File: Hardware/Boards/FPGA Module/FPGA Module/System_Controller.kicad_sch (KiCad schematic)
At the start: 32 parts, among them SW1 RST, U16 L78L33_SOT89, U5 W25Q16JVUXIQ TR, U6 RP2040, Y1 12Mhz

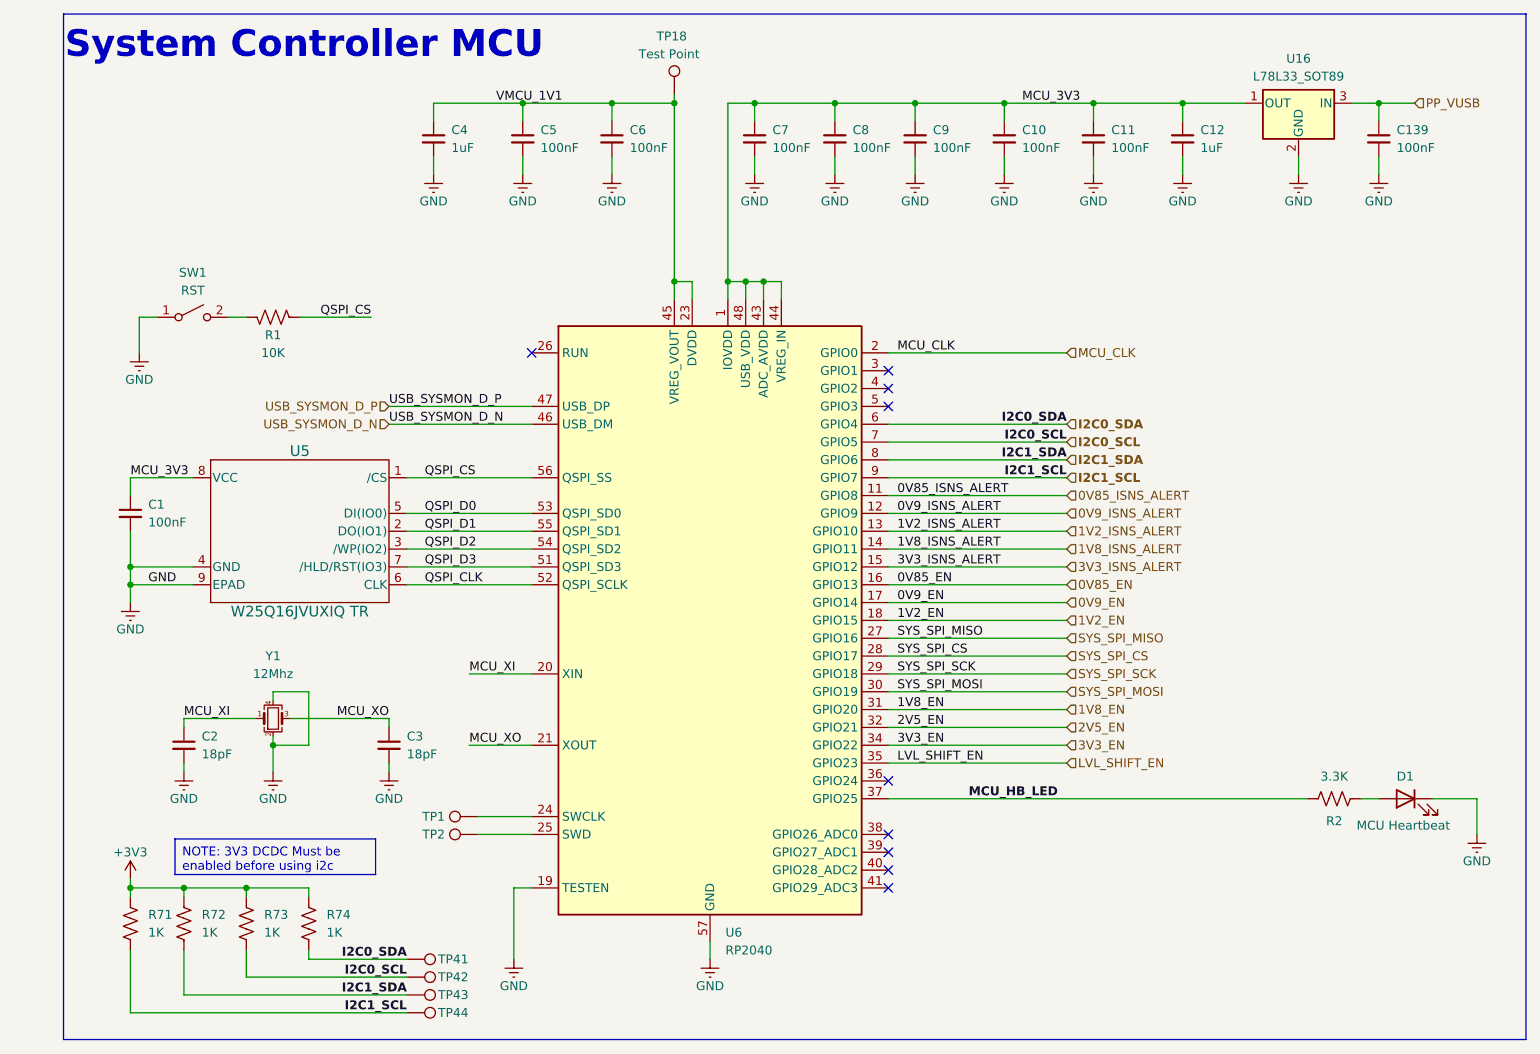
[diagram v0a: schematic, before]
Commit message: Completed FPGA module PCB layout
Started PCB routing
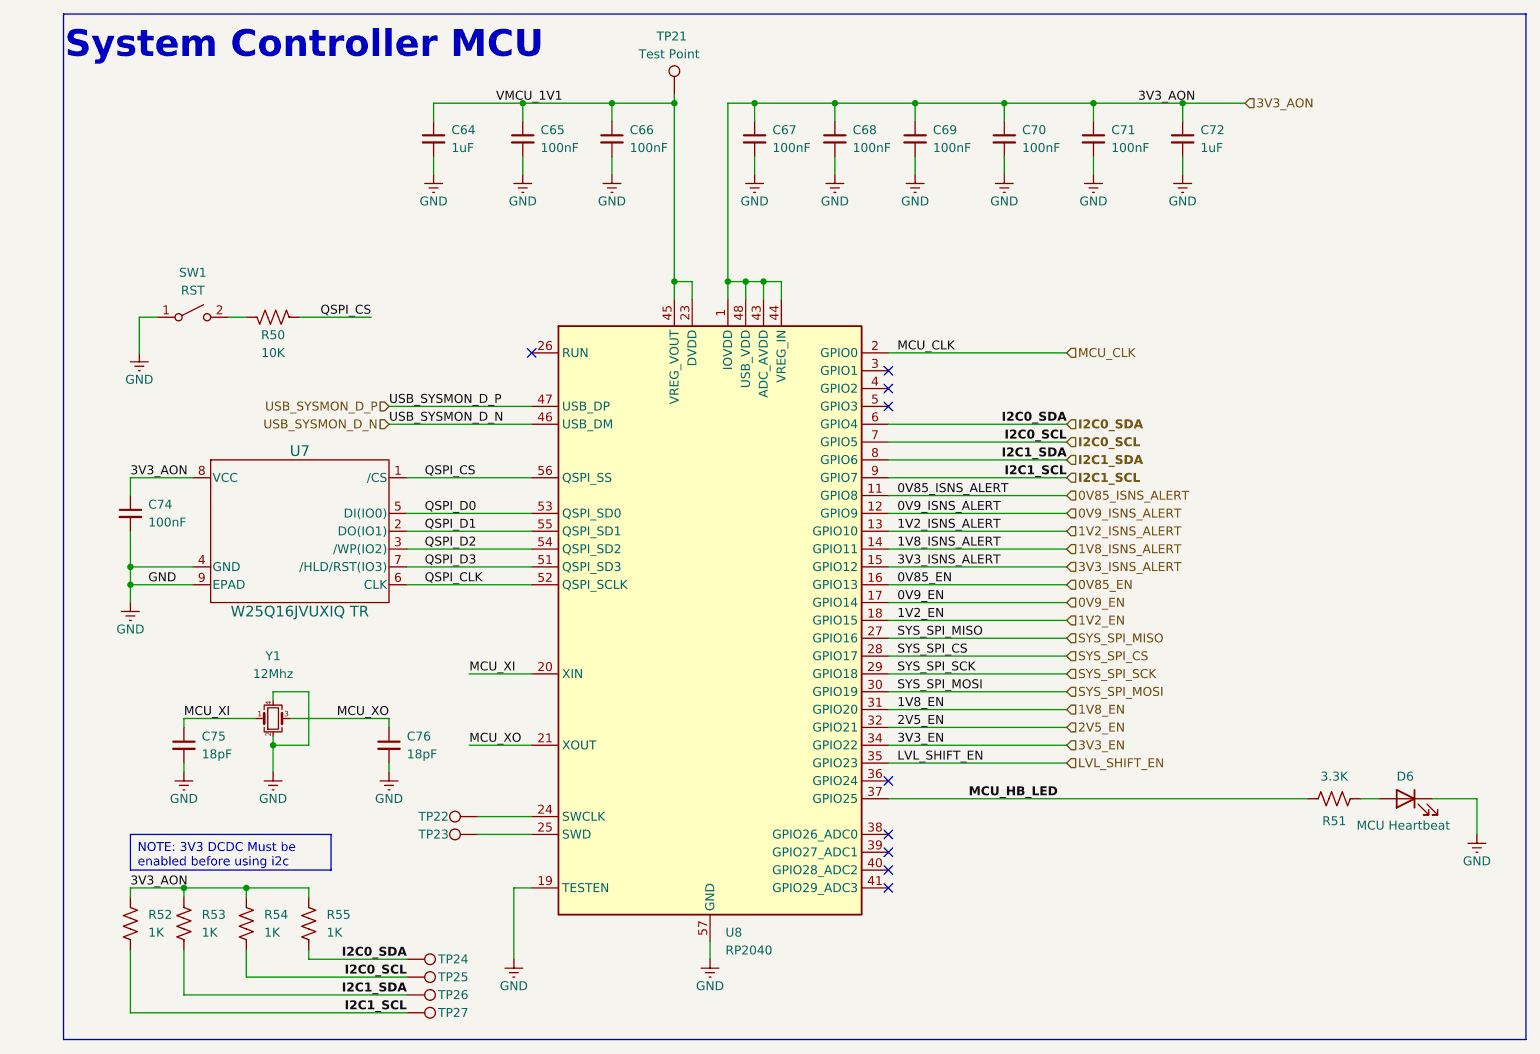
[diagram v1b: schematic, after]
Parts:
- removed C139: 100nF, Capacitor_SMD:C_0201_0603Metric, symbol Device:C_Small
- removed U16: L78L33_SOT89, Package_TO_SOT_SMD:SOT-89-3, symbol Regulator_Linear:L78L33_SOT89
- R52: renamed from R71; footprint Resistor_SMD:R_0402_1005Metric -> Resistor_SMD:R_0201_0603Metric
- R53: renamed from R72; footprint Resistor_SMD:R_0402_1005Metric -> Resistor_SMD:R_0201_0603Metric
- R54: renamed from R73; footprint Resistor_SMD:R_0402_1005Metric -> Resistor_SMD:R_0201_0603Metric
- R55: renamed from R74; footprint Resistor_SMD:R_0402_1005Metric -> Resistor_SMD:R_0201_0603Metric
- U7: renamed from U5; footprint IO_Module:USON-8_UX_2x3x0p6_WIN -> FPGA Module:USON-8_UX_2x3x0p6_WIN
- renumbered C4 to C64, C5 to C65, C6 to C66, C7 to C67, C8 to C68, C9 to C69, C10 to C70, C11 to C71, C12 to C72, C1 to C74, C2 to C75, C3 to C76, D1 to D6, R1 to R50, R2 to R51, TP18 to TP21, TP1 to TP22, TP2 to TP23, TP41 to TP24, TP42 to TP25, TP43 to TP26, TP44 to TP27, U6 to U8
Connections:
- net MCU_3V3 is gone; now on net 3V3_AON: C67.1, C68.1, C69.1, C70.1, C71.1, C72.1, C74.1, U7.8 (VCC), U8.1 (IOVDD), U8.10 (IOVDD), U8.22 (IOVDD), U8.33 (IOVDD), U8.42 (IOVDD), U8.43 (ADC_AVDD), U8.44 (VREG_IN), U8.48 (USB_VDD), U8.49 (IOVDD)
- net +3V3 renamed 3V3_AON

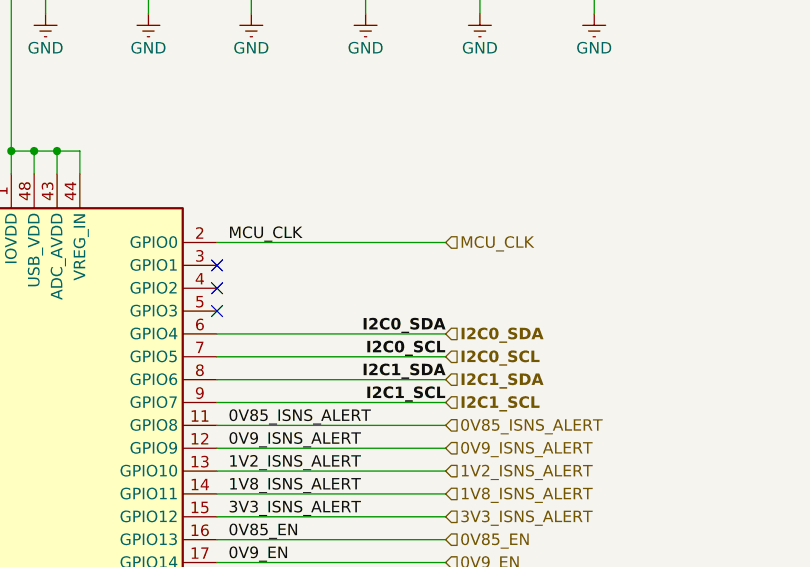
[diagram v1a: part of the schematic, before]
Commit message: Updated SCH and Layout
Added temp sensors for DCDC's, Added MCU control for FPGA mode, removed mode DIP switch
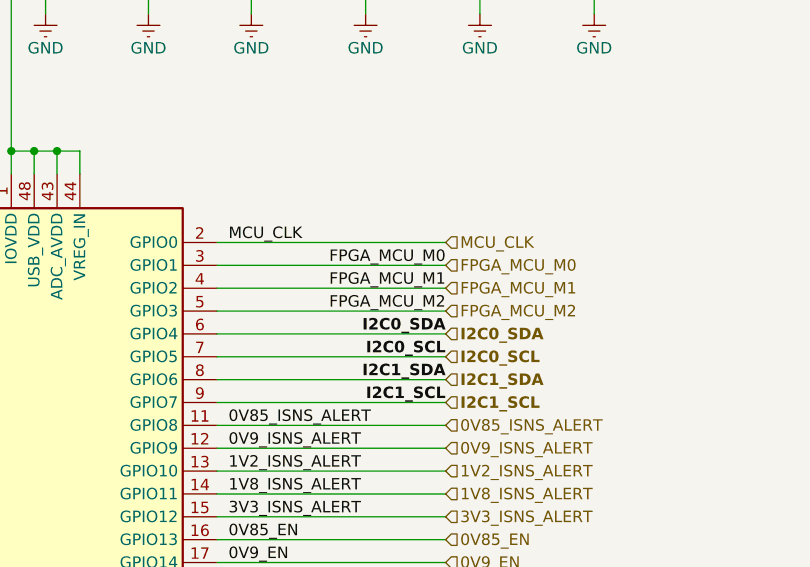
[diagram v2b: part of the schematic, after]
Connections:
- net FPGA_MCU_M0: now reaches U8.3 (GPIO1)
- net FPGA_MCU_M1: now reaches U8.4 (GPIO2)
- net FPGA_MCU_M2: now reaches U8.5 (GPIO3)
- no-connect marks 9 -> 6
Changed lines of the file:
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@@
-	)
-	(no_connect
-		(at 218.44 121.92)
 	)
 	(no_connect
@@
 	)
 	(no_connect
-		(at 218.44 119.38)
-	)
-	(no_connect
-		(at 218.44 124.46)
-	)
-	(no_connect
 		(at 167.64 116.84)
 	)
@@
 	(wire
 		(pts
+			(xy 218.44 124.46) (xy 243.84 124.46)
+		)
+		(stroke
+			(width 0)
+			(type default)
+		)
+	)
+	(wire
+		(pts
 			(xy 218.44 132.08) (xy 243.84 132.08)
 		)
@@
 	(wire
 		(pts
+			(xy 218.44 119.38) (xy 243.84 119.38)
+		)
+		(stroke
+			(width 0)
+			(type default)
+		)
+	)
+	(wire
+		(pts
 			(xy 199.39 81.28) (xy 199.39 83.82)
 		)
@@
 		(pts
 			(xy 124.46 111.76) (xy 127 111.76)
+		)
+		(stroke
+			(width 0)
+			(type default)
+		)
+	)
+	(wire
+		(pts
+			(xy 218.44 121.92) (xy 243.84 121.92)
 		)
 		(stroke
@@
 		)
 	)
+	(label "FPGA_MCU_M2"
+		(at 243.84 124.46 180)
+		(fields_autoplaced yes)
+		(effects
+			(font
+				(size 1.27 1.27)
+			)
+			(justify right bottom)
+		)
+	)
 	(label "GND"
 		(at 113.03 149.86 0)
@@
 		)
 	)
+	(label "FPGA_MCU_M0"
+		(at 243.84 119.38 180)
+		(fields_autoplaced yes)
+		(effects
+			(font
+				(size 1.27 1.27)
+			)
+			(justify right bottom)
+		)
+	)
 	(label "I2C1_SDA"
 		(at 243.84 132.08 180)
@@
 			)
 			(justify left bottom)
+		)
+	)
+	(label "FPGA_MCU_M1"
+		(at 243.84 121.92 180)
+		(fields_autoplaced yes)
+		(effects
+			(font
+				(size 1.27 1.27)
+			)
+			(justify right bottom)
 		)
 	)
@@
 		)
 	)
+	(hierarchical_label "FPGA_MCU_M0"
+		(shape input)
+		(at 243.84 119.38 0)
+		(fields_autoplaced yes)
+		(effects
+			(font
+				(size 1.27 1.27)
+			)
+			(justify left)
+		)
+	)
+	(hierarchical_label "FPGA_MCU_M2"
+		(shape input)
+		(at 243.84 124.46 0)
+		(fields_autoplaced yes)
+		(effects
+			(font
+				(size 1.27 1.27)
+			)
+			(justify left)
+		)
+	)
 	(hierarchical_label "1V2_ISNS_ALERT"
 		(shape input)
@@
 			)
 			(justify left)
+		)
+	)
+	(hierarchical_label "FPGA_MCU_M1"
+		(shape input)
+		(at 243.84 121.92 0)
+		(fields_autoplaced yes)
+		(effects
+			(font
+				(size 1.27 1.27)
+			)
+			(justify left)

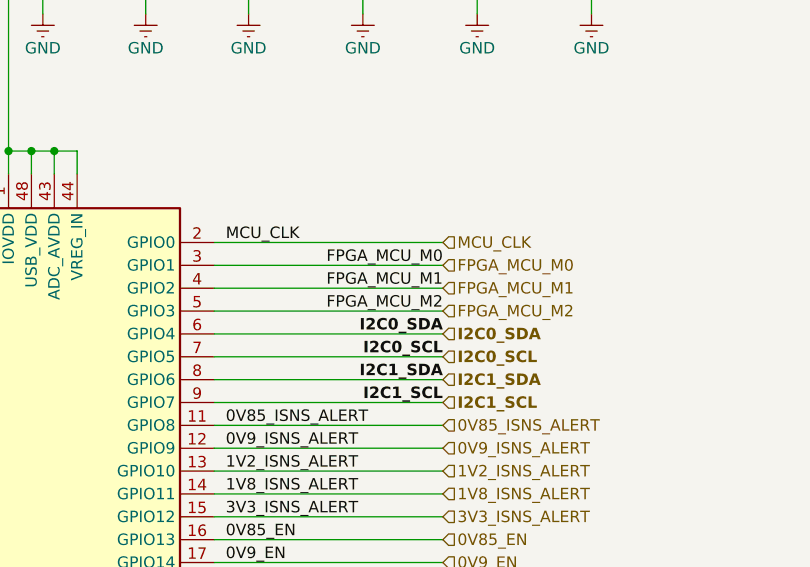
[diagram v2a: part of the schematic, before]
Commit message: FPGA Layout update
Added power panes & moved IO Buffer to MCU
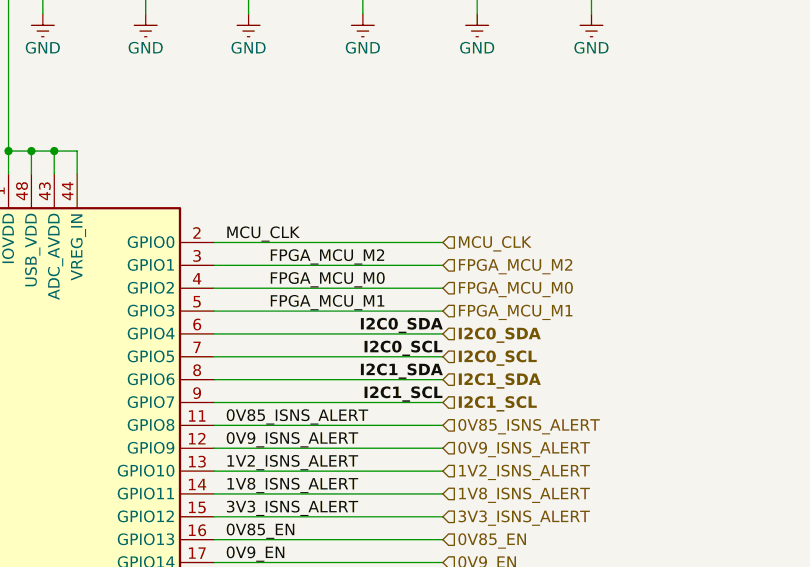
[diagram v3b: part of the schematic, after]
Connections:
- net FPGA_MCU_M0: now also U8.4 (GPIO2); no longer U8.3 (GPIO1)
- net FPGA_MCU_M1: now also U8.5 (GPIO3); no longer U8.4 (GPIO2)
- net FPGA_MCU_M2: now also U8.3 (GPIO1); no longer U8.5 (GPIO3)
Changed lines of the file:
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@@
+	(wire
+		(pts
+			(xy 243.84 119.38) (xy 218.44 119.38)
+		)
+		(stroke
+			(width 0)
+			(type default)
+		)
+	)
 	(wire
 		(pts
@@
 	(wire
 		(pts
+			(xy 243.84 124.46) (xy 218.44 124.46)
+		)
+		(stroke
+			(width 0)
+			(type default)
+		)
+	)
+	(wire
+		(pts
 			(xy 166.37 81.28) (xy 153.67 81.28)
 		)
@@
 	(wire
 		(pts
-			(xy 218.44 124.46) (xy 243.84 124.46)
-		)
-		(stroke
-			(width 0)
-			(type default)
-		)
-	)
-	(wire
-		(pts
 			(xy 218.44 132.08) (xy 243.84 132.08)
 		)
@@
 	(wire
 		(pts
-			(xy 218.44 119.38) (xy 243.84 119.38)
-		)
-		(stroke
-			(width 0)
-			(type default)
-		)
-	)
-	(wire
-		(pts
 			(xy 199.39 81.28) (xy 199.39 83.82)
 		)
@@
 	(wire
 		(pts
+			(xy 218.44 127) (xy 243.84 127)
+		)
+		(stroke
+			(width 0)
+			(type default)
+		)
+	)
+	(wire
+		(pts
 			(xy 190.5 109.22) (xy 190.5 106.68)
 		)
@@
 	(wire
 		(pts
-			(xy 218.44 127) (xy 243.84 127)
-		)
-		(stroke
-			(width 0)
-			(type default)
-		)
-	)
-	(wire
-		(pts
 			(xy 247.65 81.28) (xy 260.35 81.28)
 		)
@@
 	(wire
 		(pts
+			(xy 243.84 121.92) (xy 218.44 121.92)
+		)
+		(stroke
+			(width 0)
+			(type default)
+		)
+	)
+	(wire
+		(pts
 			(xy 247.65 81.28) (xy 247.65 83.82)
 		)
@@
 		(pts
 			(xy 124.46 111.76) (xy 127 111.76)
-		)
-		(stroke
-			(width 0)
-			(type default)
-		)
-	)
-	(wire
-		(pts
-			(xy 218.44 121.92) (xy 243.84 121.92)
 		)
 		(stroke
@@
 		)
 	)
+	(label "FPGA_MCU_M1"
+		(at 237.49 124.46 180)
+		(fields_autoplaced yes)
+		(effects
+			(font
+				(size 1.27 1.27)
+			)
+			(justify right bottom)
+		)
+	)
 	(label "USB_SYSMON_D_P"
 		(at 147.32 124.46 0)
@@
 		)
 	)
-	(label "FPGA_MCU_M2"
-		(at 243.84 124.46 180)
-		(fields_autoplaced yes)
-		(effects
-			(font
-				(size 1.27 1.27)
-			)
-			(justify right bottom)
-		)
-	)
 	(label "GND"
 		(at 113.03 149.86 0)
@@
 	)
 	(label "FPGA_MCU_M0"
-		(at 243.84 119.38 180)
+		(at 237.49 121.92 180)
+		(fields_autoplaced yes)
+		(effects
+			(font
+				(size 1.27 1.27)
+			)
+			(justify right bottom)
+		)
+	)
+	(label "FPGA_MCU_M2"
+		(at 237.49 119.38 180)
 		(fields_autoplaced yes)
 		(effects
@@
 		)
 	)
-	(label "FPGA_MCU_M1"
-		(at 243.84 121.92 180)
-		(fields_autoplaced yes)
-		(effects
-			(font
-				(size 1.27 1.27)
-			)
-			(justify right bottom)
-		)
-	)
 	(label "I2C0_SCL"
 		(at 149.86 205.74 180)
@@
 		)
 	)
+	(hierarchical_label "FPGA_MCU_M2"
+		(shape input)
+		(at 243.84 119.38 0)
+		(fields_autoplaced yes)
+		(effects
+			(font
+				(size 1.27 1.27)
+			)
+			(justify left)
+		)
+	)
 	(hierarchical_label "0V9_EN"
 		(shape input)
@@
 		)
 	)
+	(hierarchical_label "1V2_ISNS_ALERT"
+		(shape input)
+		(at 243.84 142.24 0)
+		(fields_autoplaced yes)
+		(effects
+			(font
+				(size 1.27 1.27)
+			)
+			(justify left)
+		)
+	)
+	(hierarchical_label "LVL_SHIFT_EN"
+		(shape input)
+		(at 243.84 175.26 0)
+		(fields_autoplaced yes)
+		(effects
+			(font
+				(size 1.27 1.27)
+			)
+			(justify left)
+		)
+	)
+	(hierarchical_label "0V85_ISNS_ALERT"
+		(shape input)
+		(at 243.84 137.16 0)
+		(fields_autoplaced yes)
+		(effects
+			(font
+				(size 1.27 1.27)
+			)
+			(justify left)
+		)
+	)
+	(hierarchical_label "I2C1_SDA"
+		(shape input)
+		(at 243.84 132.08 0)
+		(fields_autoplaced yes)
+		(effects
+			(font
+				(size 1.27 1.27)
+				(bold yes)
+			)
+			(justify left)
+		)
+	)
+	(hierarchical_label "SYS_SPI_CS"
+		(shape input)
+		(at 243.84 160.02 0)
+		(fields_autoplaced yes)
+		(effects
+			(font
+				(size 1.27 1.27)
+			)
+			(justify left)
+		)
+	)
+	(hierarchical_label "I2C0_SDA"
+		(shape input)
+		(at 243.84 127 0)
+		(fields_autoplaced yes)
+		(effects
+			(font
+				(size 1.27 1.27)
+				(bold yes)
+			)
+			(justify left)
+		)
+	)
+	(hierarchical_label "3V3_AON"
+		(shape input)
+		(at 269.24 81.28 0)
+		(fields_autoplaced yes)
+		(effects
+			(font
+				(size 1.27 1.27)
+			)
+			(justify left)
+		)
+	)
+	(hierarchical_label "1V8_EN"
+		(shape input)
+		(at 243.84 167.64 0)
+		(fields_autoplaced yes)
+		(effects
+			(font
+				(size 1.27 1.27)
+			)
+			(justify left)
+		)
+	)
+	(hierarchical_label "0V9_ISNS_ALERT"
+		(shape input)
+		(at 243.84 139.7 0)
+		(fields_autoplaced yes)
+		(effects
+			(font
+				(size 1.27 1.27)
+			)
+			(justify left)
+		)
+	)
+	(hierarchical_label "1V2_EN"
+		(shape input)
+		(at 243.84 154.94 0)
+		(fields_autoplaced yes)
+		(effects
+			(font
+				(size 1.27 1.27)
+			)
+			(justify left)
+		)
+	)
+	(hierarchical_label "FPGA_MCU_M1"
+		(shape input)
+		(at 243.84 124.46 0)
+		(fields_autoplaced yes)
+		(effects
+			(font
+				(size 1.27 1.27)
+			)
+			(justify left)
+		)
+	)
+	(hierarchical_label "3V3_EN"
+		(shape input)
+		(at 243.84 172.72 0)
+		(fields_autoplaced yes)
+		(effects
+			(font
+				(size 1.27 1.27)
+			)
+			(justify left)
+		)
+	)
 	(hierarchical_label "FPGA_MCU_M0"
 		(shape input)
-		(at 243.84 119.38 0)
-		(fields_autoplaced yes)
-		(effects
-			(font
-				(size 1.27 1.27)
-			)
-			(justify left)
-		)
-	)
-	(hierarchical_label "FPGA_MCU_M2"
-		(shape input)
-		(at 243.84 124.46 0)
-		(fields_autoplaced yes)
-		(effects
-			(font
-				(size 1.27 1.27)
-			)
-			(justify left)
-		)
-	)
-	(hierarchical_label "1V2_ISNS_ALERT"
-		(shape input)
-		(at 243.84 142.24 0)
-		(fields_autoplaced yes)
-		(effects
-			(font
-				(size 1.27 1.27)
-			)
-			(justify left)
-		)
-	)
-	(hierarchical_label "LVL_SHIFT_EN"
-		(shape input)
-		(at 243.84 175.26 0)
-		(fields_autoplaced yes)
-		(effects
-			(font
-				(size 1.27 1.27)
-			)
-			(justify left)
-		)
-	)
-	(hierarchical_label "0V85_ISNS_ALERT"
-		(shape input)
-		(at 243.84 137.16 0)
-		(fields_autoplaced yes)
-		(effects
-			(font
-				(size 1.27 1.27)
-			)
-			(justify left)
-		)
-	)
-	(hierarchical_label "I2C1_SDA"
-		(shape input)
-		(at 243.84 132.08 0)
-		(fields_autoplaced yes)
-		(effects
-			(font
-				(size 1.27 1.27)
-				(bold yes)
-			)
-			(justify left)
-		)
-	)
-	(hierarchical_label "FPGA_MCU_M1"
-		(shape input)
 		(at 243.84 121.92 0)
 		(fields_autoplaced yes)
 		(effects
-			(font
-				(size 1.27 1.27)
-			)
-			(justify left)
-		)
-	)
-	(hierarchical_label "SYS_SPI_CS"
-		(shape input)
-		(at 243.84 160.02 0)
-		(fields_autoplaced yes)
-		(effects
-			(font
-				(size 1.27 1.27)
-			)
-			(justify left)
-		)
-	)
-	(hierarchical_label "I2C0_SDA"
-		(shape input)
-		(at 243.84 127 0)
-		(fields_autoplaced yes)
-		(effects
-			(font
-				(size 1.27 1.27)
-				(bold yes)
-			)
-			(justify left)
-		)
-	)
-	(hierarchical_label "3V3_AON"
-		(shape input)
-		(at 269.24 81.28 0)
-		(fields_autoplaced yes)
-		(effects
-			(font
-				(size 1.27 1.27)
-			)
-			(justify left)
-		)
-	)
-	(hierarchical_label "1V8_EN"
-		(shape input)
-		(at 243.84 167.64 0)
-		(fields_autoplaced yes)
-		(effects
-			(font
-				(size 1.27 1.27)
-			)
-			(justify left)
-		)
-	)
-	(hierarchical_label "0V9_ISNS_ALERT"
-		(shape input)
-		(at 243.84 139.7 0)
-		(fields_autoplaced yes)
-		(effects
-			(font
-				(size 1.27 1.27)
-			)
-			(justify left)
-		)
-	)
-	(hierarchical_label "1V2_EN"
-		(shape input)
-		(at 243.84 154.94 0)
-		(fields_autoplaced yes)
-		(effects
-			(font
-				(size 1.27 1.27)
-			)
-			(justify left)
-		)
-	)
-	(hierarchical_label "3V3_EN"
-		(shape input)
-		(at 243.84 172.72 0)
-		(fields_autoplaced yes)
-		(effects
